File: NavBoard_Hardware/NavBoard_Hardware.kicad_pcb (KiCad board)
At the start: 2 copper layers, 61 x 100 mm, 52 parts, among them J1 Conn_Coaxial, U2 ATMEGA328P-Project_Library, U3 OKI, U4 OKI, U5 FGPMMOPA6H, Y1 Crystal

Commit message: saved
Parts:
- added D11: LED, LED_SMD:LED_0603_1608Metric_Pad1.05x0.95mm_HandSolder, F.Cu at (91.5, 74.5)
- added D12: 1N4148, Diode_THT:D_DO-35_SOD27_P7.62mm_Horizontal, F.Cu at (87.4, 72.4)
- added Q1: BSS138, Package_TO_SOT_SMD:SOT-23, F.Cu at (88.1, 75.4)
- added Q2: BSS138, Package_TO_SOT_SMD:SOT-23, F.Cu at (97.9, 72.9)
- added R16: 500, Resistor_SMD:R_0603_1608Metric_Pad1.05x0.95mm_HandSolder, F.Cu at (88.0, 78.0)
- added R17: 10K, Resistor_SMD:R_0603_1608Metric_Pad1.05x0.95mm_HandSolder, F.Cu at (94.9, 75.4)
- added R18: 10K, Resistor_SMD:R_0603_1608Metric_Pad1.05x0.95mm_HandSolder, F.Cu at (91.4, 78.0)
- added R19: 10K, Resistor_SMD:R_0603_1608Metric_Pad1.05x0.95mm_HandSolder, F.Cu at (91.5, 76.0)
- added R20: 10K, Resistor_SMD:R_0603_1608Metric_Pad1.05x0.95mm_HandSolder, F.Cu at (94.7, 77.5)
- added R21: 10K, Resistor_SMD:R_0603_1608Metric_Pad1.05x0.95mm_HandSolder, F.Cu at (98.2, 75.4)
- added R22: 30K, Resistor_SMD:R_0603_1608Metric_Pad1.05x0.95mm_HandSolder, F.Cu at (94.7, 79.0)
- added R23: 0, Resistor_SMD:R_0603_1608Metric_Pad1.05x0.95mm_HandSolder, F.Cu at (98.1, 76.9)
- Conn4: value Molex_SL_04-MRDT_Connectors -> Molex_SL_04
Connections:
- C1 pad 1: +3V3 -> +5V
- R2 pad 1: +3V3 -> +5V
- R5 pad 1: Programming_TX -> Programming_RX
- R6 pad 1: Programming_RX -> Programming_TX
- U1 pad PA6: Net-(U1-PadPA6) -> TIVA_RX
- U1 pad PC7: IMU_TX -> TIVA_TX
- U1 pad PL0: LIDAR_SDA -> Net-(U1-PadPL0)
- U1 pad PL1: LIDAR_SCL -> Net-(U1-PadPL1)
- U2 pad 20: +3V3 -> +5V
- U2 pad 4: Net-(U2-Pad4) -> TIVAtoATM_RX
- U2 pad 5: Net-(U2-Pad5) -> TIVAtoATM_TX
- U2 pad 7: +3V3 -> +5V

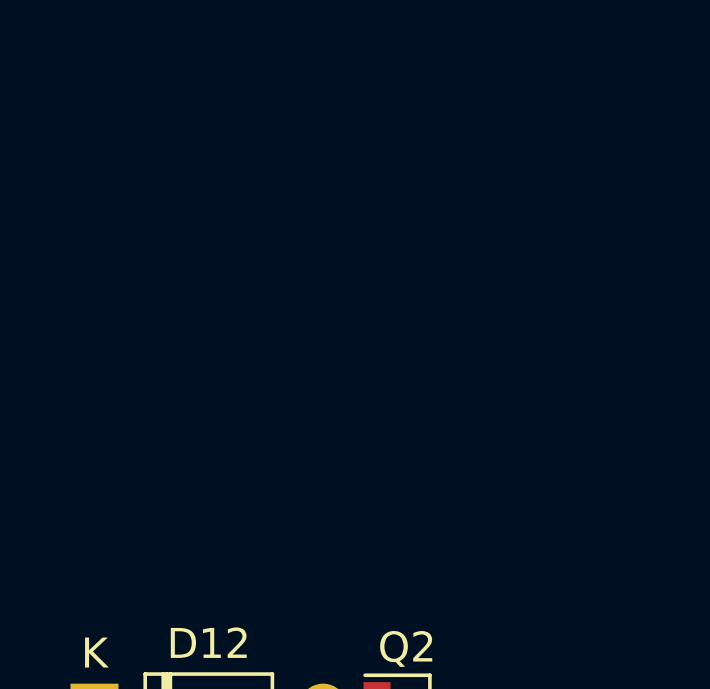
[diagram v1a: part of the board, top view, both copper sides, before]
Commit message: molex 2 added
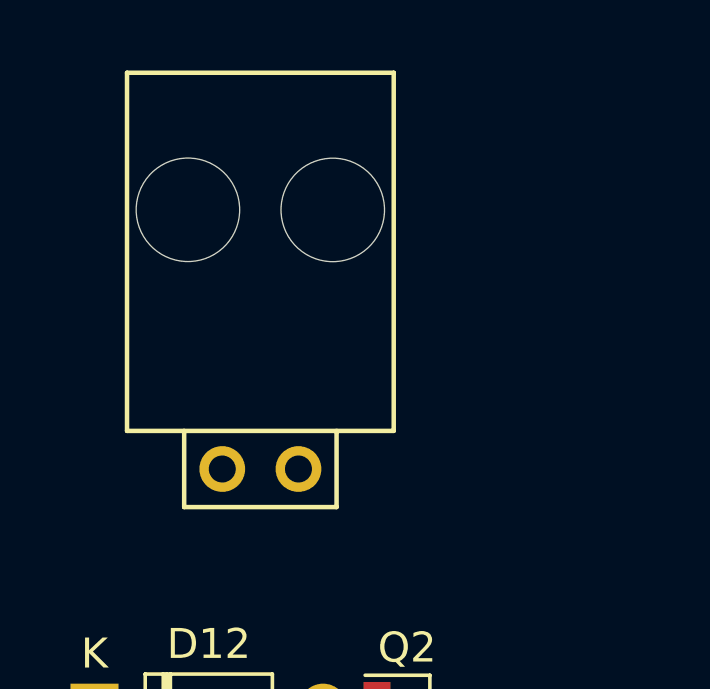
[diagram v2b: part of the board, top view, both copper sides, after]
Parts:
- added Conn3: Molex_SL-02, MRDT_Connectors:MOLEX_SL_02_Horizontal, F.Cu at (93.0, 64.4)
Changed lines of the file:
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@@
-(kicad_pcb (version 20171130) (host pcbnew "(5.0.2)-1")
+(kicad_pcb (version 20171130) (host pcbnew "(5.0.0)")
   (general
     (thickness 1.6)
@@
     (tracks 380)
     (zones 0)
-    (modules 64)
+    (modules 65)
     (nets 95)
   )
@@
     )
   )
+  (module MRDT_Connectors:MOLEX_SL_02_Horizontal (layer F.Cu)
+    (at 92.964 64.4398)
+    (fp_text reference Conn3 (at 0 2.54) (layer F.SilkS) hide
+      (effects (font (size 1 1) (thickness 0.15)))
+    )
+    (fp_text value Molex_SL-02 (at 1.27 2.286) (layer F.Fab)
+      (effects (font (size 1 1) (thickness 0.15)))
+    )
+    (fp_line (start -4.445 -1.27) (end 4.445 -1.27) (layer F.SilkS) (width 0.15))
+    (fp_line (start 4.445 -1.27) (end 4.445 -13.208) (layer F.SilkS) (width 0.15))
+    (fp_line (start 2.54 1.27) (end -2.54 1.27) (layer F.SilkS) (width 0.15))
+    (fp_line (start -4.445 -13.208) (end 4.445 -13.208) (layer F.SilkS) (width 0.15))
+    (fp_line (start -4.445 -1.27) (end -4.445 -13.208) (layer F.SilkS) (width 0.15))
+    (fp_line (start 2.54 -1.27) (end 2.54 1.27) (layer F.SilkS) (width 0.15))
+    (fp_line (start -2.54 1.27) (end -2.54 -1.27) (layer F.SilkS) (width 0.15))
+    (pad "" np_thru_hole circle (at -2.415 -8.64) (size 3.45 3.45) (drill 3.45) (layers *.Cu *.Mask))
+    (pad 1 thru_hole circle (at -1.27 0) (size 1.524 1.524) (drill 0.9) (layers *.Cu *.Mask)
+      (net 1 GND))
+    (pad 2 thru_hole circle (at 1.27 0) (size 1.524 1.524) (drill 0.9) (layers *.Cu *.Mask)
+      (net 24 IMU_RX))
+    (pad "" np_thru_hole circle (at 2.413 -8.636) (size 3.45 3.45) (drill 3.45) (layers *.Cu *.Mask))
+    (model "${MRDT_KICAD_LIBRARIES}/3D Files/MRDT_Connctors/Molex_SL_02_Horizontal.stp"
+      (offset (xyz 3.809999942779541 12.95399980545044 0))
+      (scale (xyz 1 1 1))
+      (rotate (xyz 0 0 180))
+    )
+  )

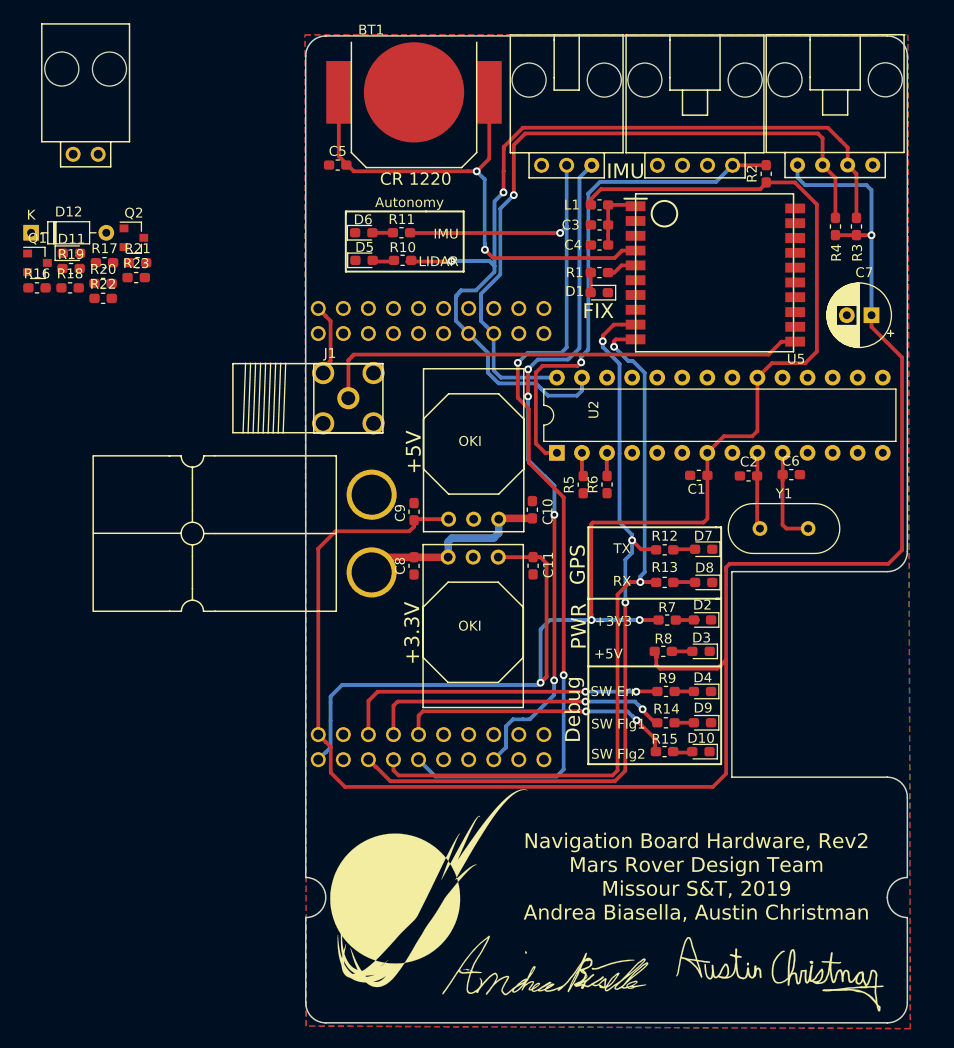
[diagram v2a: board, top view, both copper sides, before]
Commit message: Added level shifter to board and made traces beautiful
I, Andre did alot. I sleep now
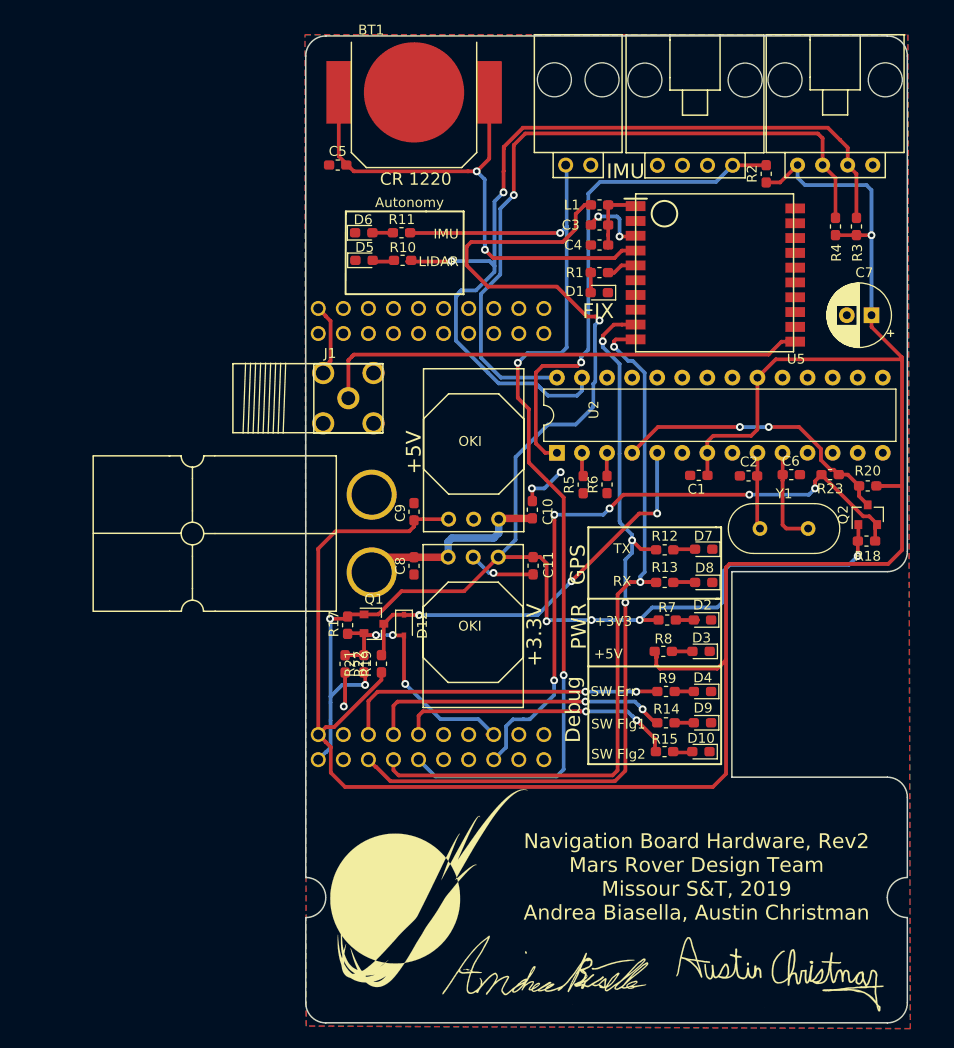
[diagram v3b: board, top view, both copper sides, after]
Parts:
- removed Conn5: Molex_SL_03, MRDT_Connectors:MOLEX_SL_03_Horizontal
- removed D11: LED, LED_SMD:LED_0603_1608Metric_Pad1.05x0.95mm_HandSolder
- removed R16: 500, Resistor_SMD:R_0603_1608Metric_Pad1.05x0.95mm_HandSolder
- D12: footprint Diode_THT:D_DO-35_SOD27_P7.62mm_Horizontal -> Diode_SMD:D_SOD-323
- moved R18 84.7 mm to (172.1, 103.6)
- moved R20 80.1 mm to (172.2, 98.0), turned to 180 degrees
- moved Q2 79.5 mm to (172.2, 101.0), turned to 90 degrees
- moved R23 73.1 mm to (168.4, 96.9), turned to 180 degrees
- moved D12 54.8 mm to (125.2, 112.1), turned to 270 degrees
- moved R19 50.9 mm to (122.9, 116.1), turned to 90 degrees
- moved Q1 50.0 mm to (122.2, 112.0)
- moved Conn3 49.9 mm to (142.9, 65.5)
- moved R21 46.7 mm to (121.2, 116.1), turned to 90 degrees
- moved R22 44.4 mm to (119.3, 116.1), turned to 270 degrees
- moved R17 44.2 mm to (119.5, 112.2), turned to 270 degrees
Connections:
- Conn3 pad 1: GND -> IMU_RX
- Conn3 pad 2: IMU_RX -> GND
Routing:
- net IMU_TX: track 69.3 -> 0.00 mm, vias 4 -> 0
- net TIVA_TX: track 0.00 -> 67.1 mm, vias 0 -> 5
- net +5V: track 178.7 -> 224.4 mm
- net TIVAtoATM_TX: track 0.00 -> 41.8 mm, vias 0 -> 3
- net TIVAtoATM_RX: track 0.00 -> 29.5 mm, vias 0 -> 2
- net TIVA_RX: track 0.00 -> 26.7 mm, vias 0 -> 3
- net GND: track 7.39 -> 29.5 mm, vias 0 -> 6
- net +3V3: track 150.7 -> 154.9 mm, vias 3 -> 7
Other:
- board text added: "2 1"
- board text removed: "3 2 1"
- board text removed: "IMU_TX"

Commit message: Fine tooth comb
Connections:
- Conn4 pad 2: Programing_RX -> Programming_RX
- Conn4 pad 3: Programing_TX -> Programming_TX
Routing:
- net Programming_TX: track 0.00 -> 63.8 mm, vias 0 -> 2
- net Programming_RX: track 0.00 -> 42.2 mm, vias 0 -> 2
- net +3V3: track 154.9 -> 136.1 mm, vias 7 -> 10
- net GND: track 29.5 -> 34.8 mm
- net TIVAtoATM_RX: track 29.5 -> 31.4 mm
- net GPS_RX: track 79.6 -> 81.2 mm
- net IMU_RX: track 99.4 -> 97.9 mm
- net TIVA_TX: track 67.1 -> 66.1 mm

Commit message: PCB UPDATES
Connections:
- net TIVAtoATM_RX renamed ATM_RX
- net TIVAtoATM_TX renamed ATM_TX
- Conn4 pad 2: Programming_RX -> Programing_RX
- Conn4 pad 3: Programming_TX -> Programing_TX
- U1 pad PA6: TIVA_RX -> IMU_RX
- U1 pad PC6: IMU_RX -> TIVA_RX
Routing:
- net TIVA_RX: track 26.7 -> 24.2 mm
- net IMU_RX: track 97.9 -> 95.8 mm
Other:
- board text added: "IMU RX"
- board text added: "Navigation Board, Rev2 Mars Rover Design Team Missouri S&T, 2019 Andrea Biasella, Austin Christman"
- board text removed: "Navigation Board Hardware, Rev2 Mars Rover Design Team Missour S&T, 2019 Andrea Biasella, Austin Christman"

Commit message: REV 2
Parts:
- moved C3 1.64 mm to (143.8, 72.7), turned to 90 degrees
- moved C4 1.25 mm to (145.8, 72.7), turned to 90 degrees
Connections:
- Conn4 pad 2: Programing_RX -> Programming_RX
- Conn4 pad 3: Programing_TX -> Programming_TX
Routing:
- net Programming_TX: track 63.8 -> 46.6 mm
- net GND: track 34.8 -> 26.9 mm, vias 6 -> 4
- net ATM_RX: track 31.4 -> 32.7 mm
- net Programming_RX: track 42.2 -> 41.3 mm
- net +5V: track 224.4 -> 223.8 mm

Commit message: final push
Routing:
- net +5V: track 223.8 -> 224.4 mm
- net +3V3: vias 10 -> 9
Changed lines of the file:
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@@
     (thickness 1.6)
     (drawings 70)
-    (tracks 544)
+    (tracks 546)
     (zones 0)
     (modules 62)
@@
   )
   (setup
-    (last_trace_width 0.381)
+    (last_trace_width 0.762)
     (user_trace_width 0.381)
     (user_trace_width 0.508)
@@
   (segment (start 138.303 105.2576) (end 139.0396 105.2576) (width 0.381) (layer F.Cu) (net 3))
   (segment (start 149.1035 111.633) (end 144.2212 111.633) (width 0.381) (layer B.Cu) (net 3))
-  (via (at 144.2212 111.633) (size 0.8) (drill 0.4) (layers F.Cu B.Cu) (net 3))
   (segment (start 119.723 111.064) (end 119.507 111.28) (width 0.381) (layer F.Cu) (net 3))
   (segment (start 121.174 111.064) (end 119.723 111.064) (width 0.381) (layer F.Cu) (net 3))
   (segment (start 171.262 103.58) (end 171.21 103.632) (width 0.381) (layer F.Cu) (net 3))
   (segment (start 171.262 101.965) (end 171.262 103.58) (width 0.381) (layer F.Cu) (net 3))
-  (segment (start 171.21 103.632) (end 171.21 105.1389) (width 0.381) (layer F.Cu) (net 3))
-  (via (at 171.196 105.1529) (size 0.8) (drill 0.4) (layers F.Cu B.Cu) (net 3))
-  (segment (start 171.21 105.1389) (end 171.196 105.1529) (width 0.381) (layer F.Cu) (net 3))
   (segment (start 170.3039 106.045) (end 171.196 105.1529) (width 0.381) (layer B.Cu) (net 3))
   (segment (start 150.3735 110.363) (end 156.972 110.363) (width 0.381) (layer B.Cu) (net 3))
@@
   (segment (start 142.621 70.4836) (end 142.621 73.1774) (width 0.381) (layer F.Cu) (net 3))
   (segment (start 143.534 69.5706) (end 142.621 70.4836) (width 0.381) (layer F.Cu) (net 3))
+  (via (at 171.196 104.521) (size 0.8) (drill 0.4) (layers F.Cu B.Cu) (net 3))
+  (segment (start 171.2494 103.632) (end 171.2494 104.4676) (width 0.381) (layer F.Cu) (net 3))
+  (segment (start 171.2494 104.4676) (end 171.196 104.521) (width 0.381) (layer F.Cu) (net 3))
+  (segment (start 171.196 104.521) (end 171.196 105.1529) (width 0.381) (layer B.Cu) (net 3))
   (segment (start 144.1476 78.0656) (end 144.1336 78.0796) (width 0.381) (layer F.Cu) (net 4))
   (segment (start 144.1476 76.0476) (end 144.1476 78.0656) (width 0.381) (layer F.Cu) (net 4))
@@
   (segment (start 172.593 81.9276) (end 175.6892 85.0238) (width 0.762) (layer F.Cu) (net 7))
   (segment (start 175.6892 104.5464) (end 174.2922 105.9434) (width 0.762) (layer F.Cu) (net 7))
-  (segment (start 157.8584 127.2032) (end 157.8584 115.6716) (width 0.762) (layer F.Cu) (net 7))
-  (segment (start 156.518581 128.543019) (end 157.8584 127.2032) (width 0.762) (layer F.Cu) (net 7))
   (segment (start 117.295199 124.000799) (end 117.295199 124.003399) (width 0.508) (layer F.Cu) (net 7))
   (segment (start 116.5352 123.2408) (end 117.295199 124.000799) (width 0.508) (layer F.Cu) (net 7))
-  (segment (start 119.244019 128.543019) (end 156.518581 128.543019) (width 0.762) (layer F.Cu) (net 7))
   (segment (start 117.295199 124.003399) (end 117.8026 124.5108) (width 0.508) (layer F.Cu) (net 7))
   (segment (start 117.8026 124.5108) (end 117.8026 127.1016) (width 0.508) (layer F.Cu) (net 7))
-  (segment (start 117.8026 127.1016) (end 119.244019 128.543019) (width 0.762) (layer F.Cu) (net 7))
   (via (at 172.593 72.644) (size 0.8) (drill 0.4) (layers F.Cu B.Cu) (net 7))
   (segment (start 172.582388 72.633388) (end 172.593 72.644) (width 0.381) (layer F.Cu) (net 7))
@@
   (segment (start 122.936 117.983) (end 122.936 117.692128) (width 0.762) (layer F.Cu) (net 7))
   (segment (start 119.507 121.412) (end 122.936 117.983) (width 0.762) (layer F.Cu) (net 7))
+  (segment (start 157.8584 127.2032) (end 157.8584 115.6716) (width 0.762) (layer F.Cu) (net 7))
+  (segment (start 155.7756 129.286) (end 157.8584 127.2032) (width 0.762) (layer F.Cu) (net 7))
+  (segment (start 120.015 129.286) (end 155.7756 129.286) (width 0.762) (layer F.Cu) (net 7))
+  (segment (start 119.272019 128.543019) (end 120.015 129.286) (width 0.762) (layer F.Cu) (net 7))
+  (segment (start 117.8026 127.1016) (end 119.244019 128.543019) (width 0.762) (layer F.Cu) (net 7))
+  (segment (start 119.244019 128.543019) (end 119.272019 128.543019) (width 0.762) (layer F.Cu) (net 7))
   (segment (start 136.3472 68.58) (end 136.3726 68.5546) (width 0.381) (layer B.Cu) (net 8))
   (segment (start 167.673606 65.565606) (end 167.64 65.532) (width 0.381) (layer F.Cu) (net 8))
